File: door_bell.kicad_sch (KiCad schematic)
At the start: 77 parts, among them J1 8-10V AC/DC, J2 Speaker, J3 SWITCH1, J4 Door panel, J5 UART, J8 MicroSD, K1 HJR 1-2C, Q1 BC847, SW1 Reset, SW2 Boot, U1 NCP1117-5v, U2 MAX98357A, U3 NCP1117-3v3, U4 DS3231M, U5 MAX3232, U6 ESP32-WROVER-B, U7 74LVC2G14

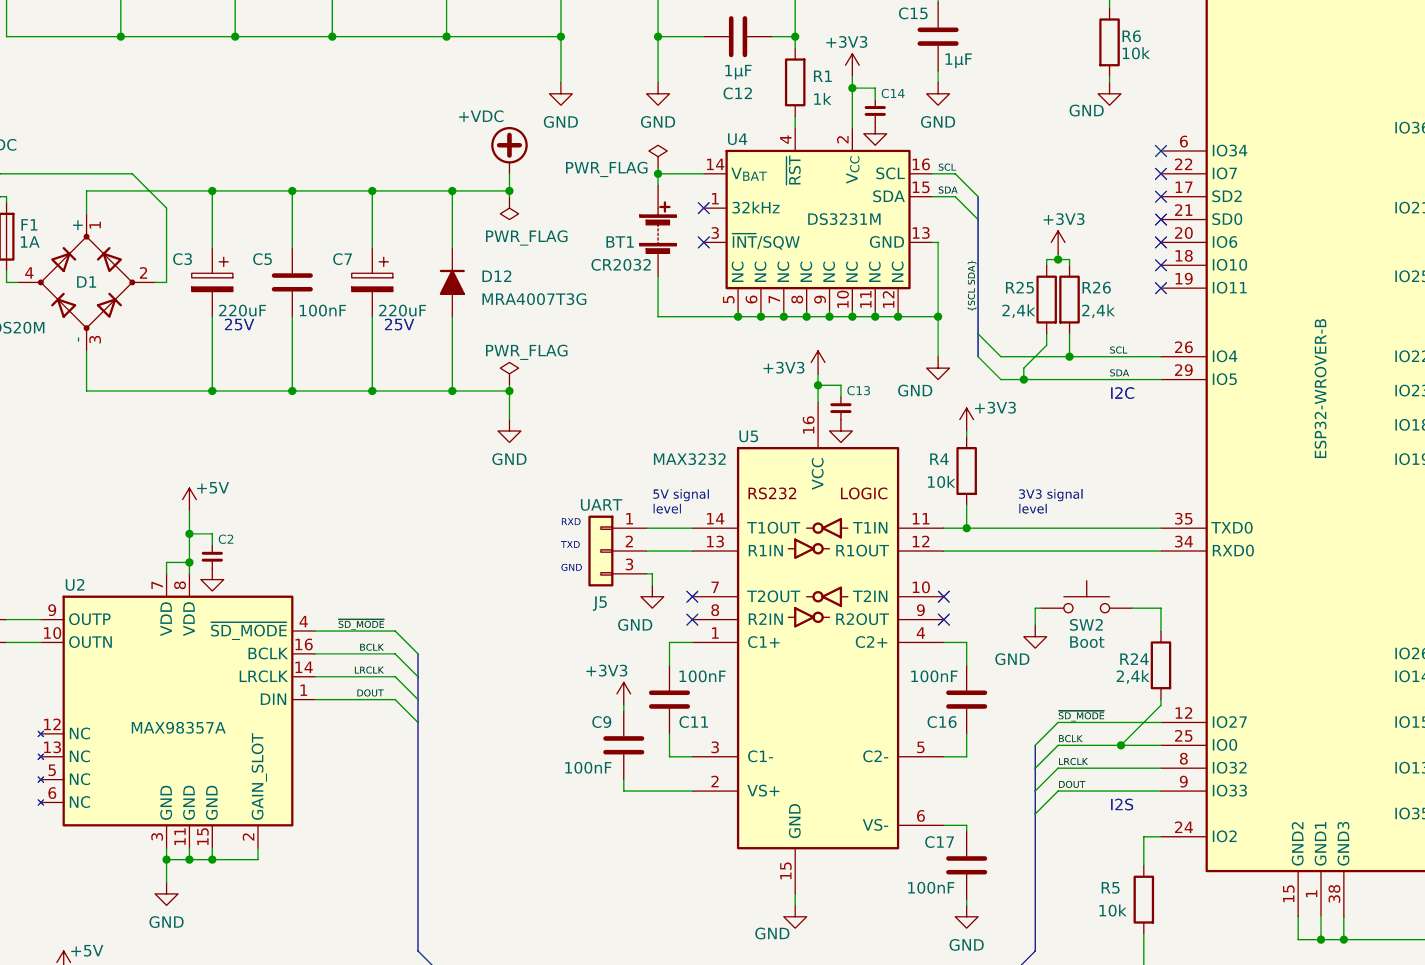
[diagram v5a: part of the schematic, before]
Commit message: Rearrange i2s pin order to eliminate wire crossing
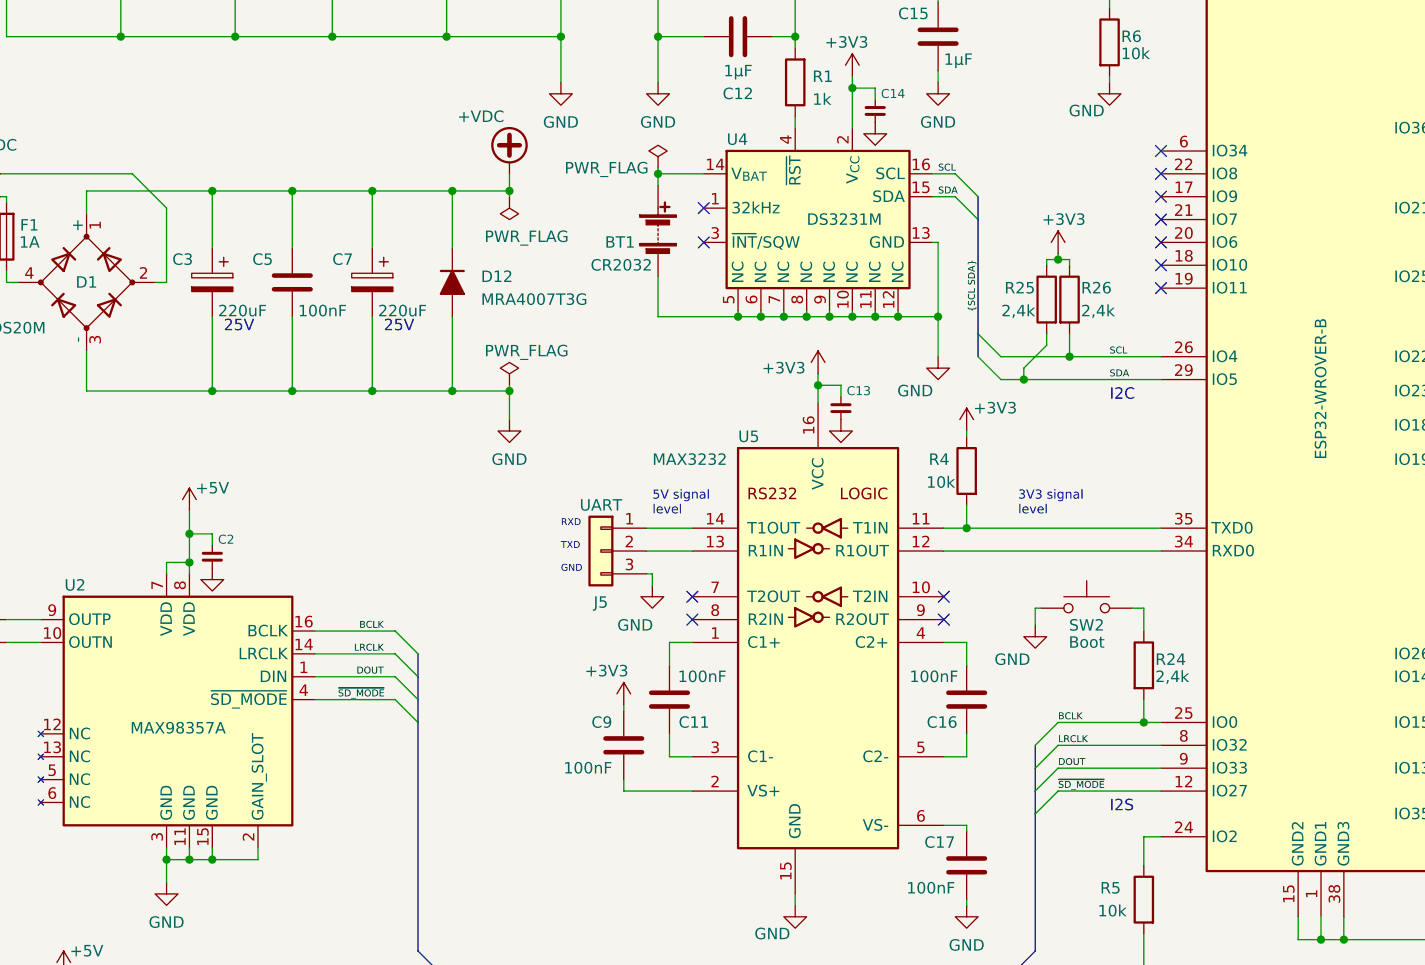
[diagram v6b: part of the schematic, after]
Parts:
- U2: footprint Package_DFN_QFN_espena:TQFN-16-1EP_3x3mm_P0.5mm_EP1.23x1.23mm -> Package_DFN_QFN:TQFN-24-1EP_4x4mm_P0.5mm_EP2.6x2.6mm
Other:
- moved on the sheet: R24
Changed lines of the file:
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@@
   (junction (at 201.93 102.87) (diameter 0) (color 0 0 0 0)
   )
+  (junction (at 156.845 127) (diameter 0) (color 0 0 0 0)
+  )
   (junction (at 66.675 28.575) (diameter 0) (color 0 0 0 0)
   )
@@
   (junction (at 133.985 40.005) (diameter 0) (color 0 0 0 0)
   )
-  (junction (at 154.305 129.54) (diameter 0) (color 0 0 0 0)
-  )
   (junction (at 61.595 28.575) (diameter 0) (color 0 0 0 0)
   )
@@
     (stroke (width 0) (type default))
   )
-  (wire (pts (xy 147.32 129.54) (xy 154.305 129.54))
+  (wire (pts (xy 147.32 129.54) (xy 158.75 129.54))
     (stroke (width 0) (type default))
   )
@@
     (stroke (width 0) (type default))
   )
+  (wire (pts (xy 156.845 124.46) (xy 156.845 127))
+    (stroke (width 0) (type default))
+  )
   (wire (pts (xy 210.82 127) (xy 213.36 127))
     (stroke (width 0) (type default))
@@
     (stroke (width 0) (type default))
   )
-  (wire (pts (xy 158.75 124.46) (xy 158.75 125.095))
-    (stroke (width 0) (type default))
-  )
   (bus (pts (xy 138.43 83.82) (xy 138.43 86.36))
     (stroke (width 0) (type default))
@@
     (stroke (width 0) (type default))
   )
-  (wire (pts (xy 147.32 127) (xy 158.75 127))
+  (wire (pts (xy 147.32 127) (xy 156.845 127))
     (stroke (width 0) (type default))
   )
@@
     (stroke (width 0) (type default))
   )
-  (wire (pts (xy 158.75 114.3) (xy 158.75 116.84))
+  (wire (pts (xy 156.845 114.3) (xy 156.845 116.84))
     (stroke (width 0) (type default))
   )
@@
     (stroke (width 0) (type default))
   )
-  (wire (pts (xy 158.75 125.095) (xy 154.305 129.54))
-    (stroke (width 0) (type default))
-  )
   (wire (pts (xy 111.76 81.915) (xy 114.3 81.915))
     (stroke (width 0) (type default))
@@
     (stroke (width 0) (type default))
   )
-  (wire (pts (xy 154.305 129.54) (xy 158.75 129.54))
-    (stroke (width 0) (type default))
-  )
   (bus (pts (xy 144.78 132.08) (xy 144.78 134.62))
     (stroke (width 0) (type default))
@@
     (stroke (width 0) (type default))
   )
+  (wire (pts (xy 156.845 127) (xy 158.75 127))
+    (stroke (width 0) (type default))
+  )
   (wire (pts (xy 207.01 102.87) (xy 212.09 102.87))
     (stroke (width 0) (type default))
@@
     (stroke (width 0) (type default))
   )
-  (wire (pts (xy 155.575 114.3) (xy 158.75 114.3))
+  (wire (pts (xy 155.575 114.3) (xy 156.845 114.3))
     (stroke (width 0) (type default))
   )
@@
     (effects (font (size 1.27 1.27)) (justify left bottom))
   )
-  (label "BCLK" (at 147.32 129.54 0) (fields_autoplaced)
+  (label "BCLK" (at 147.32 127 0) (fields_autoplaced)
     (effects (font (size 0.762 0.762)) (justify left bottom))
   )
-  (label "LRCLK" (at 72.39 121.92 180) (fields_autoplaced)
+  (label "LRCLK" (at 72.39 119.38 180) (fields_autoplaced)
     (effects (font (size 0.762 0.762)) (justify right bottom))
   )
-  (label "DOUT" (at 72.39 124.46 180) (fields_autoplaced)
+  (label "DOUT" (at 72.39 121.92 180) (fields_autoplaced)
     (effects (font (size 0.762 0.762)) (justify right bottom))
   )
-  (label "BCLK" (at 72.39 119.38 180) (fields_autoplaced)
+  (label "BCLK" (at 72.39 116.84 180) (fields_autoplaced)
     (effects (font (size 0.762 0.762)) (justify right bottom))
   )
@@
     (effects (font (size 0.762 0.762)) (justify left bottom))
   )
-  (label "~{SD_MODE}" (at 147.32 127 0) (fields_autoplaced)
+  (label "~{SD_MODE}" (at 147.32 134.62 0) (fields_autoplaced)
     (effects (font (size 0.762 0.762)) (justify left bottom))
   )
@@
     (effects (font (size 0.762 0.762)) (justify left bottom))
   )
-  (label "DOUT" (at 147.32 134.62 0) (fields_autoplaced)
+  (label "DOUT" (at 147.32 132.08 0) (fields_autoplaced)
     (effects (font (size 0.762 0.762)) (justify left bottom))
   )
@@
     (effects (font (size 0.762 0.762)) (justify left bottom))
   )
-  (label "LRCLK" (at 147.32 132.08 0) (fields_autoplaced)
+  (label "LRCLK" (at 147.32 129.54 0) (fields_autoplaced)
     (effects (font (size 0.762 0.762)) (justify left bottom))
   )
@@
     (effects (font (size 0.762 0.762)) (justify left bottom))
   )
-  (label "~{SD_MODE}" (at 67.31 116.84 0) (fields_autoplaced)
+  (label "~{SD_MODE}" (at 67.31 124.46 0) (fields_autoplaced)
     (effects (font (size 0.762 0.762)) (justify left bottom))
   )
@@
     )
   )
-  (symbol (lib_id "Device:R") (at 158.75 120.65 0) (mirror y) (unit 1)
+  (symbol (lib_id "Device:R") (at 156.845 120.65 0) (unit 1)
     (in_bom yes) (on_board yes) (dnp no)
-    (property "Reference" "R24" (at 157.48 120.015 0)
+    (property "Reference" "R24" (at 158.115 120.015 0)
       (effects (font (size 1.27 1.27)) (justify left))
     )
-    (property "Value" "2,4k" (at 157.48 121.92 0)
+    (property "Value" "2,4k" (at 158.115 121.92 0)
       (effects (font (size 1.27 1.27)) (justify left))
     )
-    (property "Footprint" "Resistor_SMD:R_0805_2012Metric_Pad1.20x1.40mm_HandSolder" (at 160.528 120.65 90)
+    (property "Footprint" "Resistor_SMD:R_0805_2012Metric_Pad1.20x1.40mm_HandSolder" (at 155.067 120.65 90)
       (effects (font (size 1.27 1.27)) hide)
     )
-    (property "Datasheet" "~" (at 158.75 120.65 0)
+    (property "Datasheet" "~" (at 156.845 120.65 0)
       (effects (font (size 1.27 1.27)) hide)
     )
@@
       (effects (font (size 1.27 1.27)))
     )
-    (property "Footprint" "Package_DFN_QFN_espena:TQFN-16-1EP_3x3mm_P0.5mm_EP1.23x1.23mm" (at 49.53 161.29 0)
+    (property "Footprint" "Package_DFN_QFN:TQFN-24-1EP_4x4mm_P0.5mm_EP2.6x2.6mm" (at 49.53 161.29 0)
       (effects (font (size 1.27 1.27)) hide)
     )

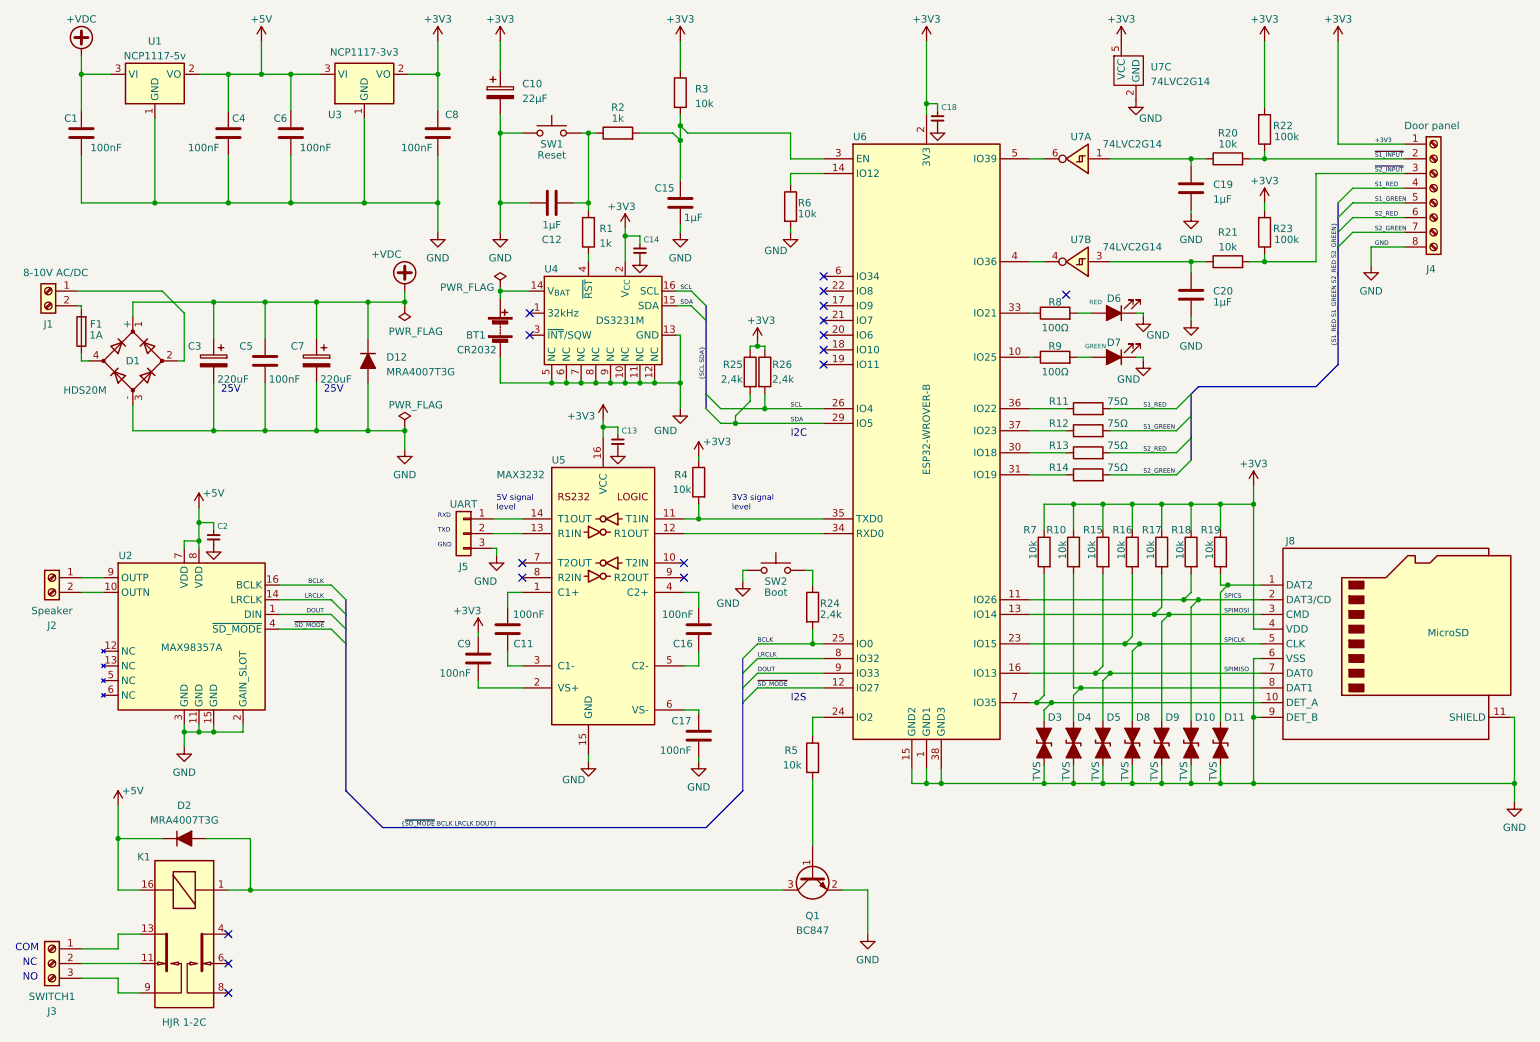
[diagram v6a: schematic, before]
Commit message: Add TVS diode and note on panel LED resistors
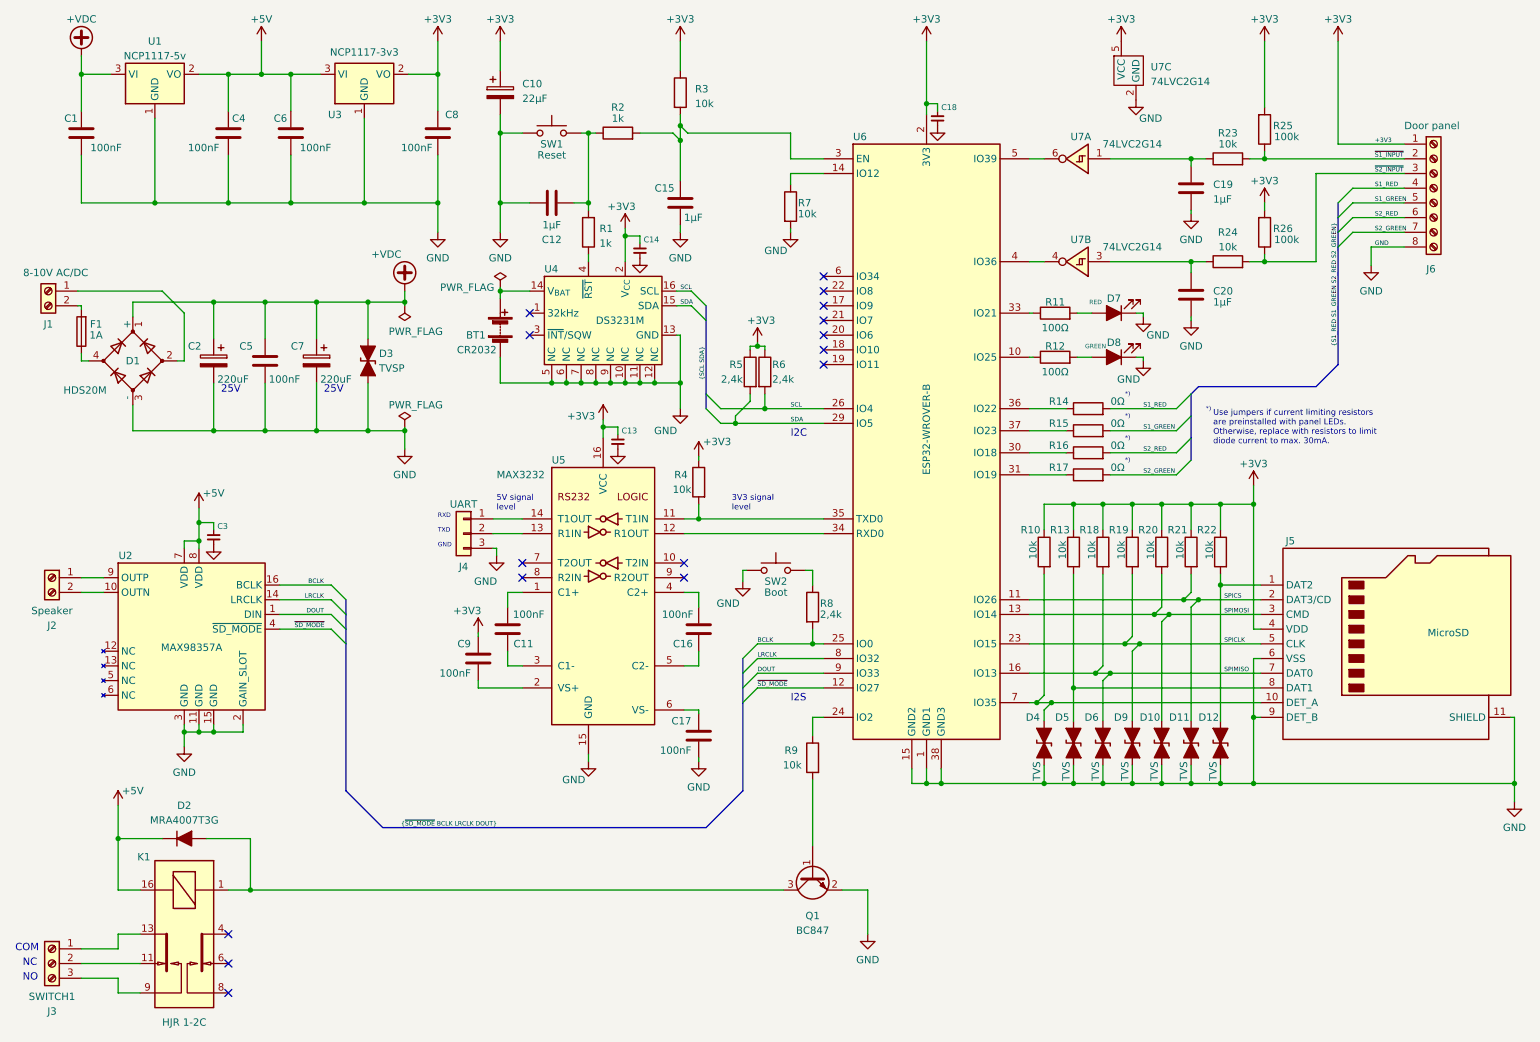
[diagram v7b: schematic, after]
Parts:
- removed D12: MRA4007T3G, Diode_SMD:D_SMB_Handsoldering, symbol Device:D_Filled
- added D3: TVSP, Diode_SMD_espena:DO-214AA-2, symbol Device:D_TVS_Filled
- R14: renamed from R11; value 75Ω -> 0Ω
- R15: renamed from R12; value 75Ω -> 0Ω
- R16: renamed from R13; value 75Ω -> 0Ω
- R17: renamed from R14; value 75Ω -> 0Ω
- renumbered C3 to C2, C2 to C3, D9 to D10, D10 to D11, D11 to D12, D3 to D4, D4 to D5, D5 to D6, D6 to D7, D7 to D8, D8 to D9, J5 to J4, J8 to J5, J4 to J6, R7 to R10, R8 to R11, R9 to R12, R10 to R13, R15 to R18, R16 to R19, R17 to R20, R18 to R21, R19 to R22, R20 to R23, R21 to R24, R22 to R25, R23 to R26, R25 to R5, R26 to R6, R6 to R7, R24 to R8, R5 to R9
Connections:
- net +VDC: now also D3.2 (A2)
- net GND: now also D3.1 (A1)
- no-connect marks 17 -> 16
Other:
- note added: "*)"
- note added: "Use jumpers if current limiting resistors are preinstalled with panel LEDs. Otherwise, replace with resistors to limit diode current to max. 30mA."
